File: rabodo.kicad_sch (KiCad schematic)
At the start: 28 parts, among them SW1 SW_Push, SW10 SW_Push, SW11 SW_Push, SW12 SW_Push, SW13 SW_Push, SW14 SW_Push, SW15 SW_Push, SW16 SW_Push, SW17 SW_Push, SW18 SW_Push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

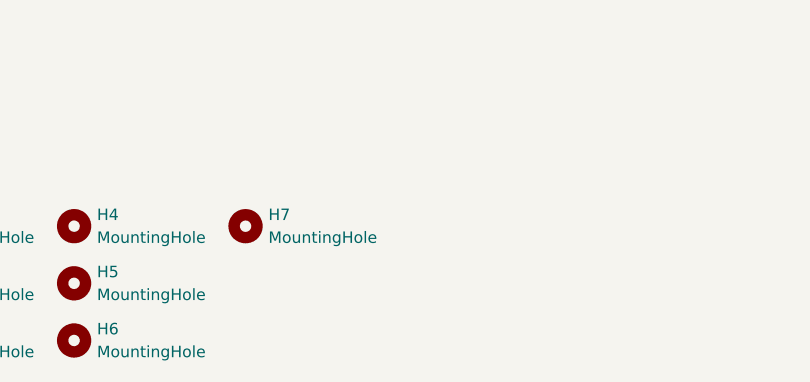
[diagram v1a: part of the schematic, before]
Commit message: Expanding and rewiring board.
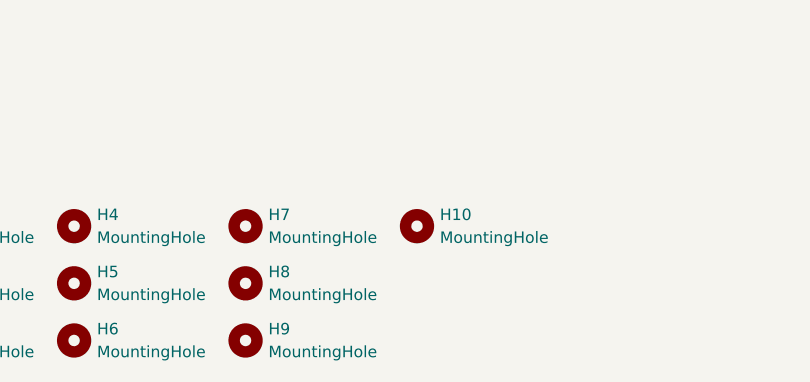
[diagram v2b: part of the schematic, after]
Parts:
- added H10, H8, H9: MountingHole, MountingHole:MountingHole_6.4mm_M6, symbol Mechanical:MountingHole
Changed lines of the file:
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@@
+    )
+  )
+  (symbol (lib_id "Mechanical:MountingHole") (at 57.15 191.77 0) (unit 1)
+    (in_bom yes) (on_board yes) (dnp no) (fields_autoplaced)
+    (property "Reference" "H9" (at 59.69 190.4999 0)
+      (effects (font (size 1.27 1.27)) (justify left))
+    )
+    (property "Value" "MountingHole" (at 59.69 193.0399 0)
+      (effects (font (size 1.27 1.27)) (justify left))
+    )
+    (property "Footprint" "MountingHole:MountingHole_6.4mm_M6" (at 57.15 191.77 0)
+      (effects (font (size 1.27 1.27)) hide)
+    )
+    (property "Datasheet" "~" (at 57.15 191.77 0)
+      (effects (font (size 1.27 1.27)) hide)
+    )
+    (instances
+      (project "rabodo"
+        (path "/476e1f68-8aac-4dba-a60f-5d5808a2f7b0"
+          (reference "H9") (unit 1)
+        )
+      )
     )
   )
@@
         (path "/476e1f68-8aac-4dba-a60f-5d5808a2f7b0"
           (reference "H7") (unit 1)
+        )
+      )
+    )
+  )
+  (symbol (lib_id "Mechanical:MountingHole") (at 76.2 179.07 0) (unit 1)
+    (in_bom yes) (on_board yes) (dnp no) (fields_autoplaced)
+    (property "Reference" "H10" (at 78.74 177.7999 0)
+      (effects (font (size 1.27 1.27)) (justify left))
+    )
+    (property "Value" "MountingHole" (at 78.74 180.3399 0)
+      (effects (font (size 1.27 1.27)) (justify left))
+    )
+    (property "Footprint" "MountingHole:MountingHole_6.4mm_M6" (at 76.2 179.07 0)
+      (effects (font (size 1.27 1.27)) hide)
+    )
+    (property "Datasheet" "~" (at 76.2 179.07 0)
+      (effects (font (size 1.27 1.27)) hide)
+    )
+    (instances
+      (project "rabodo"
+        (path "/476e1f68-8aac-4dba-a60f-5d5808a2f7b0"
+          (reference "H10") (unit 1)
         )
       )
@@
         )
       )
+    )
+  )
+  (symbol (lib_id "Mechanical:MountingHole") (at 57.15 185.42 0) (unit 1)
+    (in_bom yes) (on_board yes) (dnp no) (fields_autoplaced)
+    (property "Reference" "H8" (at 59.69 184.1499 0)
+      (effects (font (size 1.27 1.27)) (justify left))
+    )
+    (property "Value" "MountingHole" (at 59.69 186.6899 0)
+      (effects (font (size 1.27 1.27)) (justify left))
+    )
+    (property "Footprint" "MountingHole:MountingHole_6.4mm_M6" (at 57.15 185.42 0)
+      (effects (font (size 1.27 1.27)) hide)
+    )
+    (property "Datasheet" "~" (at 57.15 185.42 0)
+      (effects (font (size 1.27 1.27)) hide)
+    )
+    (instances
+      (project "rabodo"
+        (path "/476e1f68-8aac-4dba-a60f-5d5808a2f7b0"
+          (reference "H8") (unit 1)
+        )
+      )
